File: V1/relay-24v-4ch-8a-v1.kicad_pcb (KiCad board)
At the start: 2 copper layers, 53 x 67.8 mm, 22 parts, among them J1 DG141V-2.54-6P, J2 DB142V-5.08-8P, K1 G5Q-1A4-DC24V, K2 G5Q-1A4-DC24V, K3 G5Q-1A4-DC24V, K4 G5Q-1A4-DC24V

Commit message: Prefab checks
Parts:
- D1, D3, D5, D7: value GREEN -> EMERALD
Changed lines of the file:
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@@
 			)
 		)
-		(property "Value" "GREEN"
+		(property "Value" "EMERALD"
 			(at 0 1.43 0)
 			(layer "F.Fab")
@@
 			)
 		)
-		(property "LCSC Part #" "C72043"
+		(property "LCSC Part #" "C2984266"
 			(at 0 0 0)
 			(layer "F.Fab")
@@
 			)
 		)
-		(property "Mfr" "Everlight"
+		(property "Mfr" "Everlight Elec"
 			(at 0 0 0)
 			(layer "F.Fab")
@@
 			)
 		)
-		(property "Mfr PN" "19-217/GHC-YR1S2/3T"
+		(property "Mfr PN" "19-213/GHC-XS1T1N/5T"
 			(at 0 0 0)
 			(layer "F.Fab")
@@
 			)
 		)
-		(property "Vendor PN" "C72043"
+		(property "Vendor PN" "C2984266"
 			(at 0 0 0)
 			(layer "F.Fab")
@@
 			)
 		)
-		(property "Value" "GREEN"
+		(property "Value" "EMERALD"
 			(at 0 1.43 0)
 			(layer "F.Fab")
@@
 			)
 		)
-		(property "LCSC Part #" "C72043"
+		(property "LCSC Part #" "C2984266"
 			(at 0 0 0)
 			(layer "F.Fab")
@@
 			)
 		)
-		(property "Mfr" "Everlight"
+		(property "Mfr" "Everlight Elec"
 			(at 0 0 0)
 			(layer "F.Fab")
@@
 			)
 		)
-		(property "Mfr PN" "19-217/GHC-YR1S2/3T"
+		(property "Mfr PN" "19-213/GHC-XS1T1N/5T"
 			(at 0 0 0)
 			(layer "F.Fab")
@@
 			)
 		)
-		(property "Vendor PN" "C72043"
+		(property "Vendor PN" "C2984266"
 			(at 0 0 0)
 			(layer "F.Fab")
@@
 			)
 		)
-		(property "Value" "GREEN"
+		(property "Value" "EMERALD"
 			(at 0 1.43 0)
 			(layer "F.Fab")
@@
 			)
 		)
-		(property "LCSC Part #" "C72043"
+		(property "LCSC Part #" "C2984266"
 			(at 0 0 0)
 			(layer "F.Fab")
@@
 			)
 		)
-		(property "Mfr" "Everlight"
+		(property "Mfr" "Everlight Elec"
 			(at 0 0 0)
 			(layer "F.Fab")
@@
 			)
 		)
-		(property "Mfr PN" "19-217/GHC-YR1S2/3T"
+		(property "Mfr PN" "19-213/GHC-XS1T1N/5T"
 			(at 0 0 0)
 			(layer "F.Fab")
@@
 			)
 		)
-		(property "Vendor PN" "C72043"
+		(property "Vendor PN" "C2984266"
 			(at 0 0 0)
 			(layer "F.Fab")
@@
 			)
 		)
-		(property "Value" "GREEN"
+		(property "Value" "EMERALD"
 			(at 0 1.43 0)
 			(layer "F.Fab")
@@
 			)
 		)
-		(property "LCSC Part #" "C72043"
+		(property "LCSC Part #" "C2984266"
 			(at 0 0 0)
 			(layer "F.Fab")
@@
 			)
 		)
-		(property "Mfr" "Everlight"
+		(property "Mfr" "Everlight Elec"
 			(at 0 0 0)
 			(layer "F.Fab")
@@
 			)
 		)
-		(property "Mfr PN" "19-217/GHC-YR1S2/3T"
+		(property "Mfr PN" "19-213/GHC-XS1T1N/5T"
 			(at 0 0 0)
 			(layer "F.Fab")
@@
 			)
 		)
-		(property "Vendor PN" "C72043"
+		(property "Vendor PN" "C2984266"
 			(at 0 0 0)
 			(layer "F.Fab")

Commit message: Updated footprints
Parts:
- added J3: Conn_01x04, Tales:TerminalBlock_Dibo_DB142V-5.08-4P_1x04_P5.08mm_Vertical, F.Cu at (155.0, 122.6)
- J1: value DG141V-2.54-6P -> DB141V-2.54-6P
- J2: value DB142V-5.08-8P -> Conn_01x04; footprint Tales:TerminalBlock_Dibo_DB142V-5.08-8P_1x08_P5.08mm_Vertical -> Tales:TerminalBlock_Dibo_DB142V-5.08-4P_1x04_P5.08mm_Vertical
- moved J2 2.50 mm to (129.5, 122.6)
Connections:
- K3 pad 2: Net-(J2-Pin_6) -> Net-(J3-Pin_2)
- K3 pad 3: Net-(J2-Pin_5) -> Net-(J3-Pin_1)
- K4 pad 2: Net-(J2-Pin_8) -> Net-(J3-Pin_4)
- K4 pad 3: Net-(J2-Pin_7) -> Net-(J3-Pin_3)
- RV3 pad 1: Net-(J2-Pin_5) -> Net-(J3-Pin_1)
- RV3 pad 2: Net-(J2-Pin_6) -> Net-(J3-Pin_2)
- RV4 pad 1: Net-(J2-Pin_7) -> Net-(J3-Pin_3)
- RV4 pad 2: Net-(J2-Pin_8) -> Net-(J3-Pin_4)
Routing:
- net Net-(J2-Pin_8): track 66.6 -> 0.00 mm
- net Net-(J3-Pin_2): track 0.00 -> 65.4 mm
- net Net-(J2-Pin_6): track 65.1 -> 0.00 mm
- net Net-(J3-Pin_4): track 0.00 -> 64.4 mm
- net Net-(J2-Pin_7): track 47.2 -> 0.00 mm
- net Net-(J3-Pin_1): track 0.00 -> 45.9 mm
- net Net-(J2-Pin_5): track 45.7 -> 0.00 mm
- net Net-(J3-Pin_3): track 0.00 -> 45.0 mm
- net Net-(J2-Pin_2): track 66.2 -> 64.1 mm
- net Net-(J2-Pin_1): track 46.8 -> 44.7 mm
- net Net-(J2-Pin_3): track 45.2 -> 46.2 mm
- net Net-(J2-Pin_4): track 64.8 -> 65.7 mm

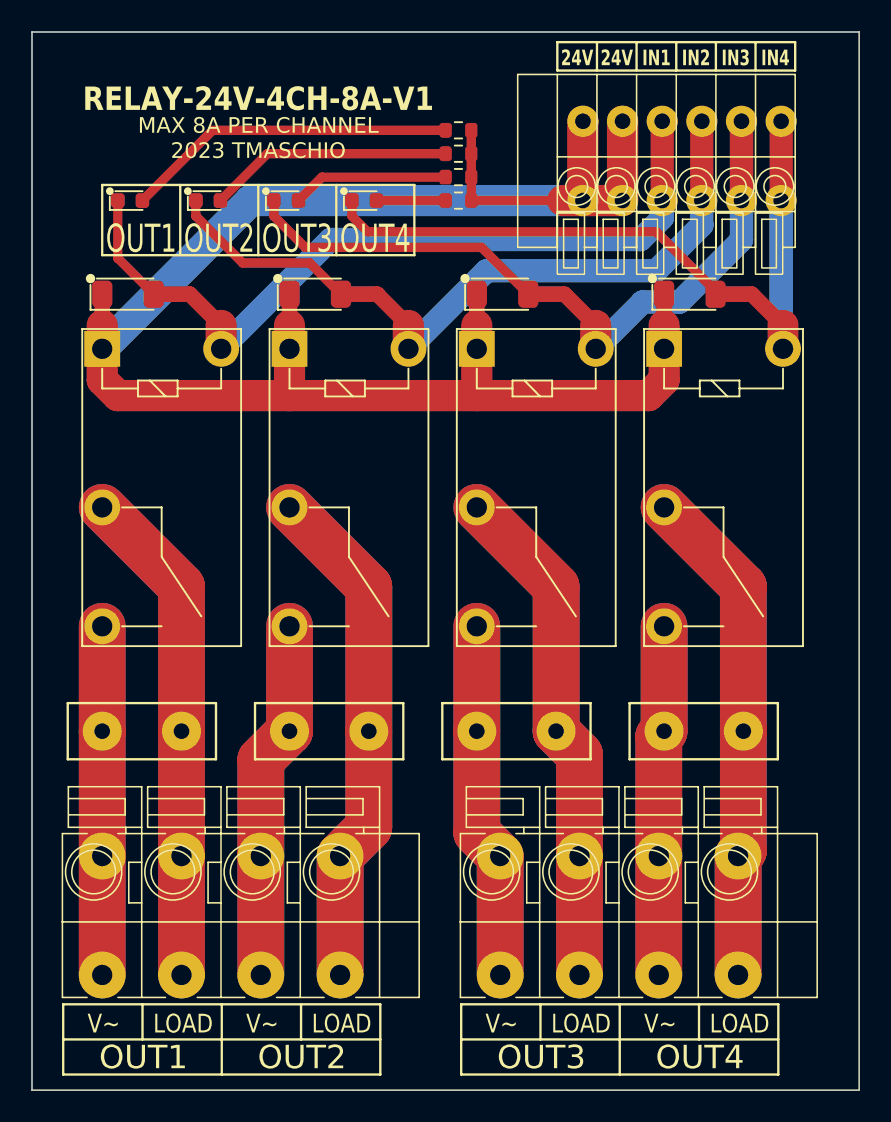
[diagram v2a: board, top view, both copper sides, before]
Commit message: Updated connectors
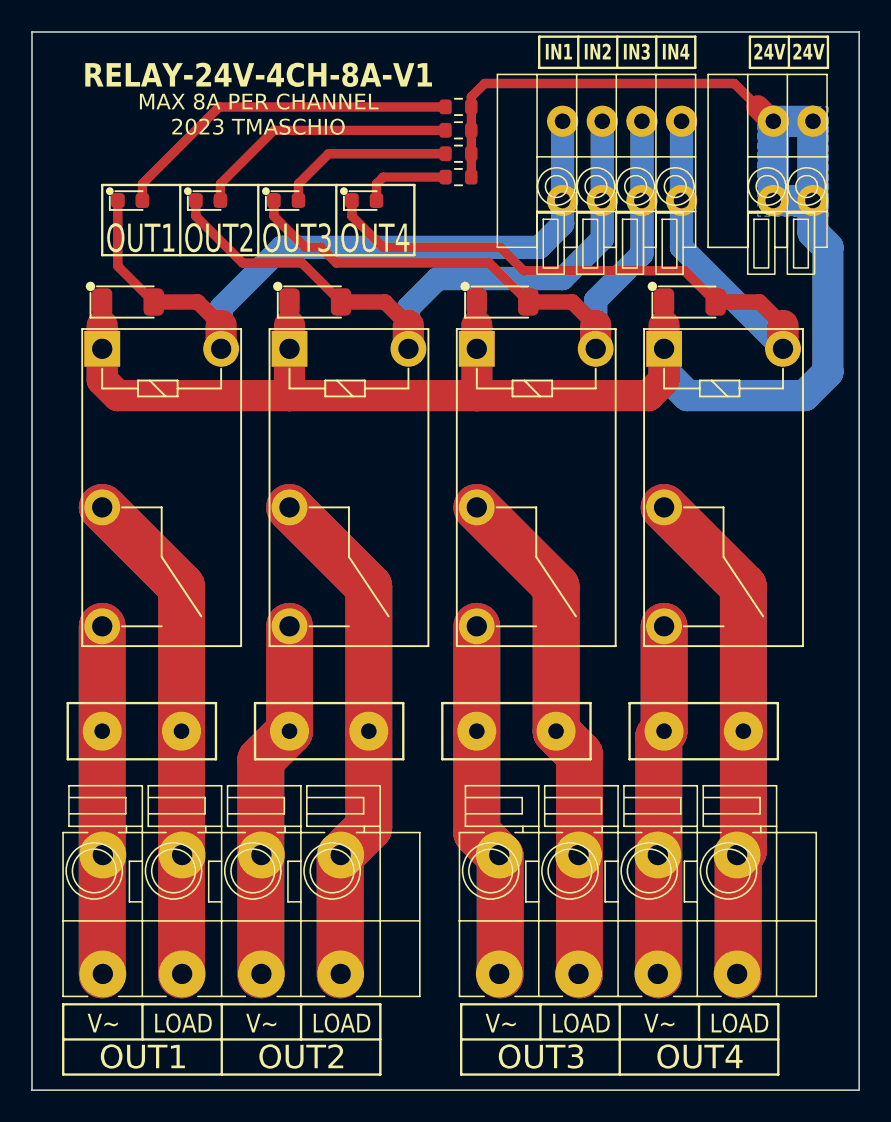
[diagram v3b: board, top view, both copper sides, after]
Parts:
- added J4: DB142V-5.08-4P, Tales:TerminalBlock_Dibo_DB142V-5.08-4P_1x04_P5.08mm_Vertical, F.Cu at (154.9, 122.6)
- J1: value DB141V-2.54-6P -> DB141V-2.54-2P; footprint Tales:TerminalBlock_Dibo_DB141V-2.54-6P_1x06_P2.54mm_Vertical -> Tales:TerminalBlock_Dibo_DB141V-2.54-2P_1x02_P2.54mm_Vertical
- J2: value Conn_01x04 -> DB141V-2.54-4P; footprint Tales:TerminalBlock_Dibo_DB142V-5.08-4P_1x04_P5.08mm_Vertical -> Tales:TerminalBlock_Dibo_DB141V-2.54-4P_1x04_P2.54mm_Vertical
- J3: value Conn_01x04 -> DB142V-5.08-4P
- R1, R2, R3, R4: value 5k6/100mW -> 6k8/100mW
- moved J2 66.1 mm to (166.6, 67.9), turned to 180 degrees
- moved J3 25.5 mm to (129.5, 122.6)
- moved J1 2.04 mm to (175.0, 67.9)
- moved R1 1.50 mm to (152.3, 67.0)
- moved R2 1.50 mm to (152.3, 68.5)
- moved R3 1.50 mm to (152.3, 70.0)
- moved R4 1.50 mm to (152.3, 71.5)
- moved D2 0.50 mm to (131.2, 79.5)
- moved D4 0.50 mm to (143.2, 79.5)
- moved D6 0.50 mm to (155.2, 79.5)
- moved D8 0.50 mm to (167.2, 79.5)
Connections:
- J1 pad 1: Net-(D7-K) -> +24V
- J1 pad 2: Net-(D5-K) -> +24V
- J2 pad 1: Net-(J2-Pin_1) -> Net-(D7-K)
- J2 pad 2: Net-(J2-Pin_2) -> Net-(D5-K)
- J2 pad 3: Net-(J2-Pin_3) -> Net-(D3-K)
- J2 pad 4: Net-(J2-Pin_4) -> Net-(D1-K)
- K1 pad 2: Net-(J2-Pin_2) -> Net-(J3-Pin_2)
- K1 pad 3: Net-(J2-Pin_1) -> Net-(J3-Pin_1)
- K2 pad 2: Net-(J2-Pin_4) -> Net-(J3-Pin_4)
- K2 pad 3: Net-(J2-Pin_3) -> Net-(J3-Pin_3)
- K3 pad 2: Net-(J3-Pin_2) -> Net-(J4-Pin_2)
- K3 pad 3: Net-(J3-Pin_1) -> Net-(J4-Pin_1)
- K4 pad 2: Net-(J3-Pin_4) -> Net-(J4-Pin_4)
- K4 pad 3: Net-(J3-Pin_3) -> Net-(J4-Pin_3)
- RV1 pad 1: Net-(J2-Pin_1) -> Net-(J3-Pin_1)
- RV1 pad 2: Net-(J2-Pin_2) -> Net-(J3-Pin_2)
- RV2 pad 1: Net-(J2-Pin_3) -> Net-(J3-Pin_3)
- RV2 pad 2: Net-(J2-Pin_4) -> Net-(J3-Pin_4)
- RV3 pad 1: Net-(J3-Pin_1) -> Net-(J4-Pin_1)
- RV3 pad 2: Net-(J3-Pin_2) -> Net-(J4-Pin_2)
- RV4 pad 1: Net-(J3-Pin_3) -> Net-(J4-Pin_3)
- RV4 pad 2: Net-(J3-Pin_4) -> Net-(J4-Pin_4)
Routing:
- net Net-(J2-Pin_4): track 65.7 -> 0.00 mm
- net Net-(J4-Pin_2): track 0.00 -> 65.4 mm
- net Net-(J4-Pin_4): track 0.00 -> 64.4 mm
- net Net-(J2-Pin_2): track 64.1 -> 0.00 mm
- net Net-(J2-Pin_3): track 46.2 -> 0.00 mm
- net Net-(J4-Pin_1): track 0.00 -> 45.9 mm
- net Net-(J4-Pin_3): track 0.00 -> 45.0 mm
- net Net-(J2-Pin_1): track 44.7 -> 0.00 mm
- net +24V: track 119.9 -> 124.6 mm
- net Net-(D1-K): track 51.5 -> 47.2 mm
- net Net-(D3-K): track 47.8 -> 43.4 mm
- net Net-(D5-K): track 45.9 -> 41.8 mm
- net Net-(D7-K): track 47.8 -> 50.3 mm
- net Net-(D5-A): track 10.0 -> 11.3 mm
- net Net-(D7-A): track 4.43 -> 5.68 mm
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- added copper zone on B.Cu, net +24V

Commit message: Revision before manufacturing
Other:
- rule pad_to_mask_clearance: 0 -> 0.1

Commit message: Revising for fabrication
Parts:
- D1, D3, D5, D7: value EMERALD -> WHITE
- R1, R2, R3, R4: value 6k8/100mW -> 10k/100mW
- moved K1 9.85 mm to (133.5, 91.5)
- moved K2 9.85 mm to (145.5, 91.5)
- moved K3 9.85 mm to (157.5, 91.5)
- moved K4 9.85 mm to (169.5, 91.5)
- moved J4 8.69 mm to (162.8, 118.8)
- moved J3 8.60 mm to (137.2, 118.8)
- moved J2 4.65 mm to (162.8, 70.5)
- moved J1 2.88 mm to (173.8, 70.5)
- moved RV1 2.75 mm to (132.2, 107.0)
- moved RV2 2.75 mm to (144.2, 107.0)
- moved RV3 2.75 mm to (156.2, 107.0)
- moved RV4 2.75 mm to (168.2, 107.0)
- moved D2 0.10 mm to (131.2, 79.5)
- moved D4 0.10 mm to (143.2, 79.5)
- moved D6 0.10 mm to (155.2, 79.5)
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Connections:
- net Net-(D1-A) renamed /LED1
- net Net-(D1-K) renamed /IN1
- net Net-(D3-A) renamed /LED2
- net Net-(D3-K) renamed /IN2
- net Net-(D5-A) renamed /LED3
- net Net-(D5-K) renamed /IN3
- net Net-(D7-A) renamed /LED4
- net Net-(D7-K) renamed /IN4
- net Net-(J3-Pin_1) renamed /OUT1PW
- net Net-(J3-Pin_2) renamed /OUT1LD
- net Net-(J3-Pin_3) renamed /OUT2PW
- net Net-(J3-Pin_4) renamed /OUT2LD
- net Net-(J4-Pin_1) renamed /OUT3PW
- net Net-(J4-Pin_2) renamed /OUT3LD
- net Net-(J4-Pin_3) renamed /OUT4PW
- net Net-(J4-Pin_4) renamed /OUT4LD
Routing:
- net +24V: track 124.6 -> 111.8 mm
- net /IN4: track 50.3 -> 58.2 mm
- net /IN2: track 43.4 -> 49.8 mm
- net /IN3: track 41.8 -> 48.1 mm
- net /IN1: track 47.2 -> 53.1 mm
- net /OUT4LD: track 64.4 -> 66.6 mm
- net /OUT2LD: track 65.7 -> 67.8 mm
- net /OUT1LD: track 64.1 -> 66.3 mm
- net /OUT3LD: track 65.4 -> 67.4 mm
- net /LED1: track 22.5 -> 23.8 mm
- net /LED2: track 16.9 -> 17.6 mm
- net /LED4: track 5.68 -> 5.01 mm
- added copper zone on F.Cu, net +24V
- removed copper zone on B.Cu, net +24V

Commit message: Revising before manufacturing.
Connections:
- net /OUT1PW renamed /OUT1LN
- net /OUT2PW renamed /OUT2LN
- net /OUT3PW renamed /OUT3LN
- net /OUT4PW renamed /OUT4LN
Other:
- board text added: "LINE"
- board text removed: "V~"
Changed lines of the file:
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@@
 	(net 9 "/IN4")
 	(net 10 "/OUT1LD")
-	(net 11 "/OUT2PW")
-	(net 12 "/OUT1PW")
+	(net 11 "/OUT2LN")
+	(net 12 "/OUT1LN")
 	(net 13 "/OUT2LD")
 	(net 14 "/OUT4LD")
-	(net 15 "/OUT3PW")
-	(net 16 "/OUT4PW")
+	(net 15 "/OUT4LN")
+	(net 16 "/OUT3LN")
 	(net 17 "/OUT3LD")
 	(footprint "Tales:TerminalBlock_Dibo_DB141V-2.54-4P_1x04_P2.54mm_Vertical"
@@
 			(layers "*.Cu" "*.Mask")
 			(remove_unused_layers no)
-			(net 15 "/OUT3PW")
+			(net 16 "/OUT3LN")
 			(pintype "passive")
 		)
@@
 			(layers "*.Cu" "*.Mask")
 			(remove_unused_layers no)
-			(net 16 "/OUT4PW")
+			(net 15 "/OUT4LN")
 			(pintype "passive")
 		)
@@
 			(layers "*.Cu" "*.Mask")
 			(remove_unused_layers no)
-			(net 12 "/OUT1PW")
+			(net 12 "/OUT1LN")
 			(pintype "passive")
 		)
@@
 			(layers "*.Cu" "*.Mask")
 			(remove_unused_layers no)
-			(net 16 "/OUT4PW")
+			(net 15 "/OUT4LN")
 			(pintype "passive")
 		)
@@
 			(layers "*.Cu" "*.Mask")
 			(remove_unused_layers no)
-			(net 11 "/OUT2PW")
+			(net 11 "/OUT2LN")
 			(pintype "passive")
 		)
@@
 			(layers "*.Cu" "*.Mask")
 			(remove_unused_layers no)
-			(net 15 "/OUT3PW")
+			(net 16 "/OUT3LN")
 			(pinfunction "Pin_1")
 			(pintype "passive")
@@
 			(layers "*.Cu" "*.Mask")
 			(remove_unused_layers no)
-			(net 15 "/OUT3PW")
+			(net 16 "/OUT3LN")
 			(pinfunction "Pin_1")
 			(pintype "passive")
@@
 			(layers "*.Cu" "*.Mask")
 			(remove_unused_layers no)
-			(net 16 "/OUT4PW")
+			(net 15 "/OUT4LN")
 			(pinfunction "Pin_3")
 			(pintype "passive")
@@
 			(layers "*.Cu" "*.Mask")
 			(remove_unused_layers no)
-			(net 16 "/OUT4PW")
+			(net 15 "/OUT4LN")
 			(pinfunction "Pin_3")
 			(pintype "passive")
@@
 			(layers "*.Cu" "*.Mask")
 			(remove_unused_layers no)
-			(net 12 "/OUT1PW")
+			(net 12 "/OUT1LN")
 			(pinfunction "Pin_1")
 			(pintype "passive")
@@
 			(layers "*.Cu" "*.Mask")
 			(remove_unused_layers no)
-			(net 12 "/OUT1PW")
+			(net 12 "/OUT1LN")
 			(pinfunction "Pin_1")
 			(pintype "passive")
@@
 			(layers "*.Cu" "*.Mask")
 			(remove_unused_layers no)
-			(net 11 "/OUT2PW")
+			(net 11 "/OUT2LN")
 			(pinfunction "Pin_3")
 			(pintype "passive")
@@
 			(layers "*.Cu" "*.Mask")
 			(remove_unused_layers no)
-			(net 11 "/OUT2PW")
+			(net 11 "/OUT2LN")
 			(pinfunction "Pin_3")
 			(pintype "passive")
@@
 			(layers "*.Cu" "*.Mask")
 			(remove_unused_layers no)
-			(net 15 "/OUT3PW")
+			(net 16 "/OUT3LN")
 			(pintype "passive")
 		)
@@
 			(layers "*.Cu" "*.Mask")
 			(remove_unused_layers no)
-			(net 11 "/OUT2PW")
+			(net 11 "/OUT2LN")
 			(pintype "passive")
 		)
@@
 			(layers "*.Cu" "*.Mask")
 			(remove_unused_layers no)
-			(net 12 "/OUT1PW")
+			(net 12 "/OUT1LN")
 			(pintype "passive")
 		)
@@
 		(layer "Edge.Cuts")
 	)
-	(gr_text "V~"
+	(gr_text "LINE"
 		(at 129.6 125.75 0)
 		(layer "F.SilkS")
@@
 		)
 	)
-	(gr_text "V~"
+	(gr_text "LINE"
 		(at 139.76 125.75 0)
 		(layer "F.SilkS")
@@
 		)
 	)
-	(gr_text "V~"
+	(gr_text "LINE"
 		(at 155.1 125.75 0)
 		(layer "F.SilkS")
@@
 		)
 	)
-	(gr_text "V~"
+	(gr_text "LINE"
 		(at 165.26 125.75 0)
 		(layer "F.SilkS")
@@
 	)
 	(segment
-		(start 155.13 114.94)
-		(end 155.13 122.56)
+		(start 165.69 100.39)
+		(end 165.69 106.98)
 		(width 3)
 		(layer "F.Cu")
@@
 	)
 	(segment
-		(start 153.71 107)
-		(end 153.71 113.52)
+		(start 165.29 114.94)
+		(end 165.29 122.56)
 		(width 3)
 		(layer "F.Cu")
@@
 	)
 	(segment
-		(start 153.71 113.52)
-		(end 155.13 114.94)
+		(start 165.29 107.42)
+		(end 165.71 107)
 		(width 3)
 		(layer "F.Cu")
@@
 	)
 	(segment
-		(start 153.69 100.39)
-		(end 153.69 106.98)
+		(start 165.29 114.94)
+		(end 165.29 107.42)
 		(width 3)
 		(layer "F.Cu")
@@
 	)
 	(segment
-		(start 153.69 106.98)
-		(end 153.71 107)
+		(start 165.69 106.98)
+		(end 165.71 107)
 		(width 3)
 		(layer "F.Cu")
@@
 	)
 	(segment
-		(start 153.69 100.39)
-		(end 153.69 106.98)
+		(start 165.69 100.39)
+		(end 165.69 106.98)
 		(width 3)
 		(layer "B.Cu")
@@
 	)
 	(segment
-		(start 153.69 106.98)
-		(end 153.71 107)
+		(start 165.29 114.94)
+		(end 165.29 122.56)
 		(width 3)
 		(layer "B.Cu")
@@
 	)
 	(segment
-		(start 155.13 114.94)
-		(end 155.13 122.56)
+		(start 165.29 107.42)
+		(end 165.29 114.94)
 		(width 3)
 		(layer "B.Cu")
@@
 	)
 	(segment
-		(start 153.71 107)
-		(end 153.71 113.52)
+		(start 165.69 106.98)
+		(end 165.71 107)
 		(width 3)
 		(layer "B.Cu")
@@
 	)
 	(segment
-		(start 153.71 113.52)
-		(end 155.13 114.94)
+		(start 165.71 107)
+		(end 165.29 107.42)
 		(width 3)
 		(layer "B.Cu")
@@
 	)
 	(segment
-		(start 165.69 100.39)
-		(end 165.69 106.98)
+		(start 155.13 114.94)
+		(end 155.13 122.56)
 		(width 3)
 		(layer "F.Cu")
@@
 	)
 	(segment
-		(start 165.29 114.94)
-		(end 165.29 122.56)
+		(start 153.71 107)
+		(end 153.71 113.52)
 		(width 3)
 		(layer "F.Cu")
@@
 	)
 	(segment
-		(start 165.29 107.42)
-		(end 165.71 107)
+		(start 153.71 113.52)
+		(end 155.13 114.94)
 		(width 3)
 		(layer "F.Cu")
@@
 	)
 	(segment
-		(start 165.29 114.94)
-		(end 165.29 107.42)
+		(start 153.69 100.39)
+		(end 153.69 106.98)
 		(width 3)
 		(layer "F.Cu")
@@
 	)
 	(segment
-		(start 165.69 106.98)
-		(end 165.71 107)
+		(start 153.69 106.98)
+		(end 153.71 107)
 		(width 3)
 		(layer "F.Cu")
@@
 	)
 	(segment
-		(start 165.69 100.39)
-		(end 165.69 106.98)
+		(start 153.69 100.39)
+		(end 153.69 106.98)
 		(width 3)
 		(layer "B.Cu")
@@
 	)
 	(segment
-		(start 165.29 114.94)
-		(end 165.29 122.56)
+		(start 153.69 106.98)
+		(end 153.71 107)
 		(width 3)
 		(layer "B.Cu")
@@
 	)
 	(segment
-		(start 165.29 107.42)
-		(end 165.29 114.94)
+		(start 155.13 114.94)
+		(end 155.13 122.56)
 		(width 3)
 		(layer "B.Cu")
@@
 	)
 	(segment
-		(start 165.69 106.98)
-		(end 165.71 107)
+		(start 153.71 107)
+		(end 153.71 113.52)
 		(width 3)
 		(layer "B.Cu")
@@
 	)
 	(segment
-		(start 165.71 107)
-		(end 165.29 107.42)
+		(start 153.71 113.52)
+		(end 155.13 114.94)
 		(width 3)
 		(layer "B.Cu")
